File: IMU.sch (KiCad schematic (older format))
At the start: 5 parts

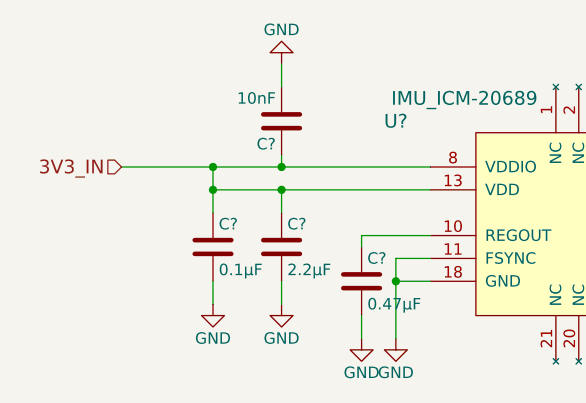
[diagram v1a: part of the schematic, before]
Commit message: added mosfet footprint some more cleanup
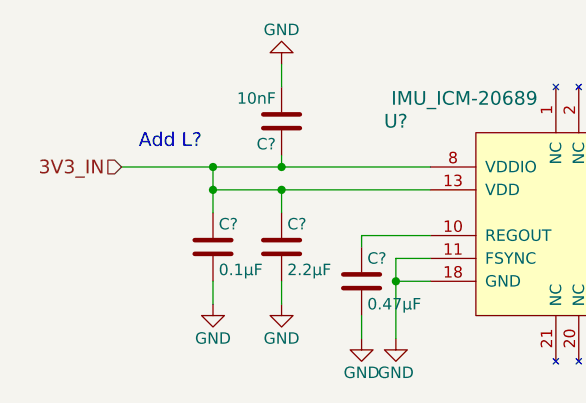
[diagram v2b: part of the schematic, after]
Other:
- note added: "Add L?"
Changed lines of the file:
@@
 Text HLabel 7400 3450 2    60   BiDi ~ 0
 INT
+Text Notes 3625 2925 0    60   ~ 0
+Add L?
 $EndSCHEMATC

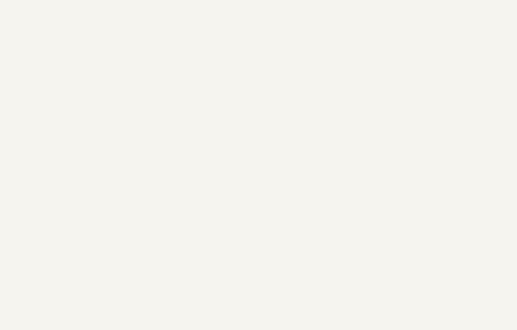
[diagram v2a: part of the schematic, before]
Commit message: added RPi Regulator added ref.des.-prefixes to all schematic sheets
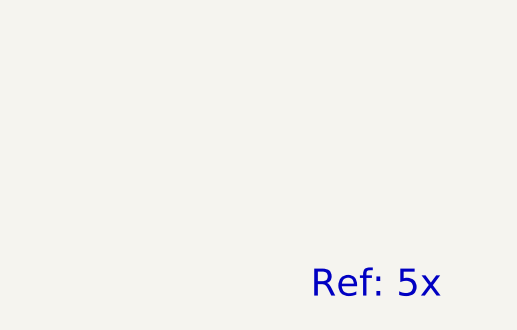
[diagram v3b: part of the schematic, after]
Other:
- note added: "Ref: 5x"
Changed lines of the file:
@@
 Text Notes 3625 2925 0    60   ~ 0
 Add L?
+Text Notes 10575 6525 0    118  ~ 0
+Ref: 5x
 $EndSCHEMATC
